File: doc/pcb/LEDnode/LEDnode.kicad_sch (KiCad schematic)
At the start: 72 parts, among them J1 Ni-MH, J2 SWD, J3 GPIO1, J4 GPIO2, Q1 PDTB113ET.215, Q2 PDTB113ET.215, Q3 PDTB113ET.215, Q4 PDTB113ET.215, Q5 IRLML6346, Q6 BSS138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

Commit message: almost working bme280
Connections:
- net +3V3: now also Q5.1 (G)
- net INPUT: no longer Q5.1 (G)
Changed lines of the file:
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@@
   (junction (at 248.285 60.96) (diameter 0) (color 0 0 0 0)
   )
+  (junction (at 46.99 19.685) (diameter 0) (color 0 0 0 0)
+  )
   (junction (at 59.69 102.87) (diameter 0) (color 0 0 0 0)
   )
@@
   (junction (at 258.445 27.305) (diameter 0) (color 0 0 0 0)
   )
-  (junction (at 46.99 19.685) (diameter 0) (color 0 0 0 0)
-  )
   (junction (at 194.945 116.205) (diameter 0) (color 0 0 0 0)
   )
@@
   )
   (junction (at 202.565 24.765) (diameter 0) (color 0 0 0 0)
-  )
-  (junction (at 31.75 19.685) (diameter 0) (color 0 0 0 0)
   )
   (junction (at 197.485 56.515) (diameter 0) (color 0 0 0 0)
@@
     (stroke (width 0) (type default) (color 0 0 0 0))
   )
+  (wire (pts (xy 46.99 13.97) (xy 46.99 19.685))
+    (stroke (width 0) (type default) (color 0 0 0 0))
+  )
   (wire (pts (xy 158.115 71.12) (xy 158.115 73.025))
     (stroke (width 0) (type default) (color 0 0 0 0))
@@
     (stroke (width 0) (type default) (color 0 0 0 0))
   )
-  (wire (pts (xy 31.75 19.685) (xy 46.99 19.685))
-    (stroke (width 0) (type default) (color 0 0 0 0))
-  )
   (wire (pts (xy 36.83 69.85) (xy 36.83 75.565))
     (stroke (width 0) (type default) (color 0 0 0 0))
@@
     (stroke (width 0) (type default) (color 0 0 0 0))
   )
+  (wire (pts (xy 19.685 19.685) (xy 19.685 13.97))
+    (stroke (width 0) (type default) (color 0 0 0 0))
+  )
   (wire (pts (xy 102.235 32.385) (xy 104.775 32.385))
     (stroke (width 0) (type default) (color 0 0 0 0))
   )
-  (wire (pts (xy 31.75 19.685) (xy 31.75 20.32))
-    (stroke (width 0) (type default) (color 0 0 0 0))
-  )
   (wire (pts (xy 250.825 57.785) (xy 250.825 60.96))
     (stroke (width 0) (type default) (color 0 0 0 0))
@@
     (stroke (width 0) (type default) (color 0 0 0 0))
   )
+  (wire (pts (xy 19.685 13.97) (xy 46.99 13.97))
+    (stroke (width 0) (type default) (color 0 0 0 0))
+  )
   (wire (pts (xy 267.335 77.47) (xy 269.24 77.47))
     (stroke (width 0) (type default) (color 0 0 0 0))
@@
   )
   (wire (pts (xy 177.8 161.29) (xy 177.8 160.655))
-    (stroke (width 0) (type default) (color 0 0 0 0))
-  )
-  (wire (pts (xy 19.685 19.685) (xy 31.75 19.685))
     (stroke (width 0) (type default) (color 0 0 0 0))
   )
@@
   (symbol (lib_id "Device:Q_NMOS_GSD") (at 31.75 25.4 90) (mirror x) (unit 1)
     (in_bom yes) (on_board yes)
-    (property "Reference" "Q5" (id 0) (at 32.385 15.875 90))
-    (property "Value" "IRLML6346" (id 1) (at 31.75 18.415 90))
+    (property "Reference" "Q5" (id 0) (at 35.56 20.32 90))
+    (property "Value" "IRLML6346" (id 1) (at 38.735 22.86 90))
     (property "Footprint" "Package_TO_SOT_SMD:SOT-23" (id 2) (at 29.21 30.48 0)
       (effects (font (size 1.27 1.27)) hide)
@@
     (pin "1")
     (pin "2")
+  )
+  (symbol (lib_id "power:+3V3") (at 31.75 20.32 0) (unit 1)
+    (in_bom yes) (on_board yes) (fields_autoplaced)
+    (property "Reference" "#PWR?" (id 0) (at 31.75 24.13 0)
+      (effects (font (size 1.27 1.27)) hide)
+    )
+    (property "Value" "+3V3" (id 1) (at 31.75 16.7442 0))
+    (property "Footprint" "" (id 2) (at 31.75 20.32 0)
+      (effects (font (size 1.27 1.27)) hide)
+    )
+    (property "Datasheet" "" (id 3) (at 31.75 20.32 0)
+      (effects (font (size 1.27 1.27)) hide)
+    )
+    (pin "1")
   )
   (symbol (lib_id "Device:R") (at 158.115 26.035 0) (unit 1)
@@
     (in_bom yes) (on_board yes)
     (property "Reference" "J1" (id 0) (at 15.24 15.909 0))
-    (property "Value" "Ni-MH" (id 1) (at 19.939 15.875 0))
+    (property "Value" "Ni-MH" (id 1) (at 15.875 13.97 0))
     (property "Footprint" "BartLib_Battery:BC-0401 AAA R3" (id 2) (at 14.605 19.685 0)
       (effects (font (size 1.27 1.27)) hide)
@@
       (reference "#PWR0148") (unit 1) (value "GND") (footprint "")
     )
+    (path "/ba6f97b6-925b-4f7e-87f5-e90895c07124"
+      (reference "#PWR?") (unit 1) (value "+3V3") (footprint "")
+    )
     (path "/c0ea8401-5770-44f1-86a5-f03597e947dd"

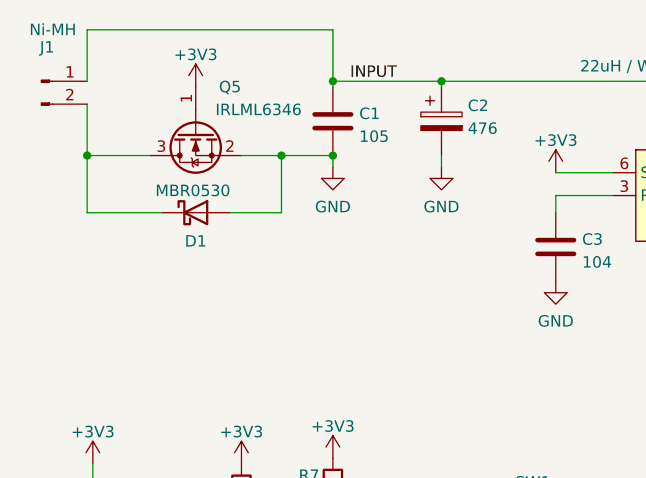
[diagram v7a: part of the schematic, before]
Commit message: corrected bme280 lib
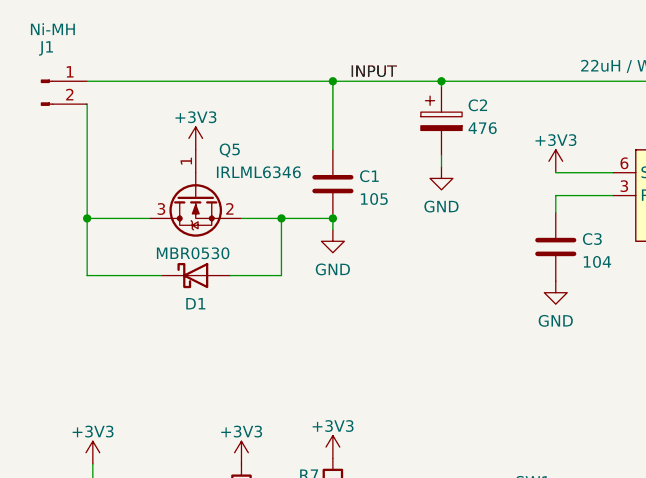
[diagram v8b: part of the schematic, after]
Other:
- moved on the sheet: C1, D1, Q5
